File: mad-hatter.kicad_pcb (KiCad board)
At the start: 2 copper layers, 337.2 x 122.6 mm, 153 parts, among them U1 ATMEGA32U4, X1 XTAL_GND

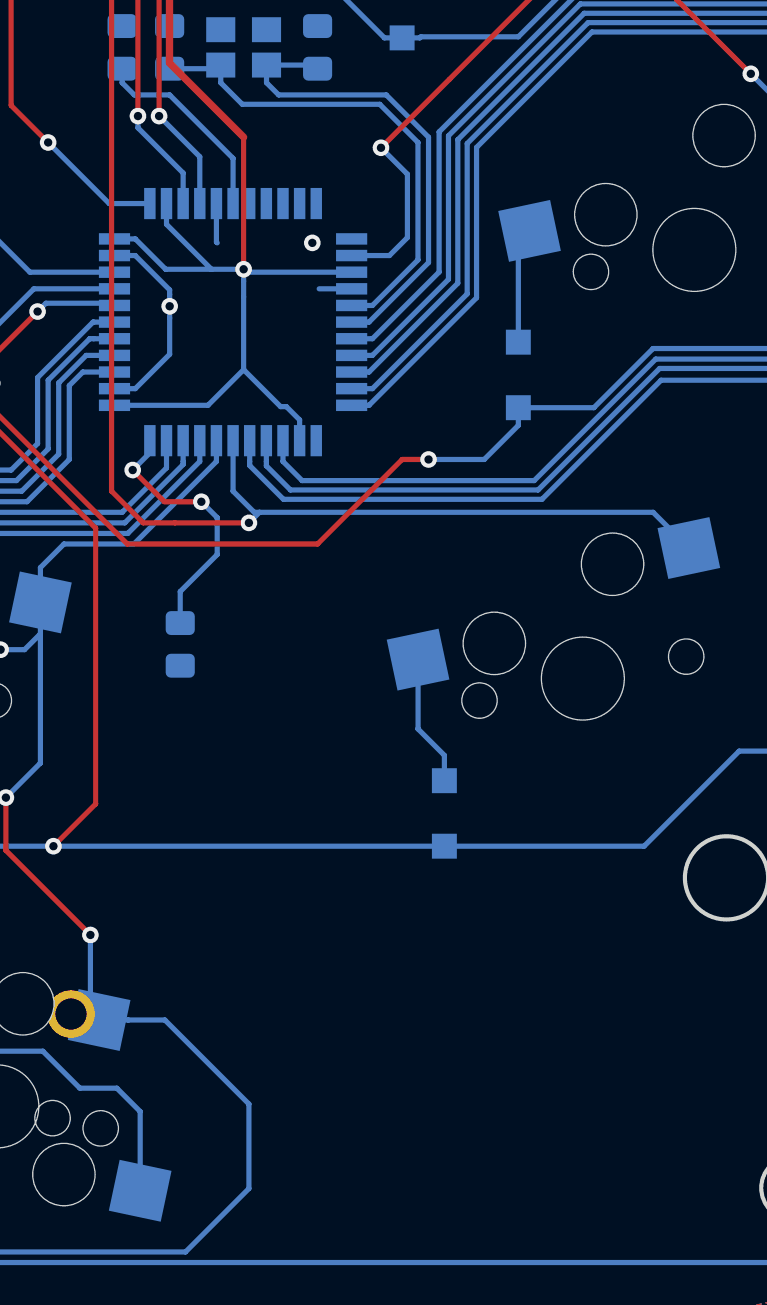
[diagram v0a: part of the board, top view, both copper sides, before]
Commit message: Starts adding ISP pads
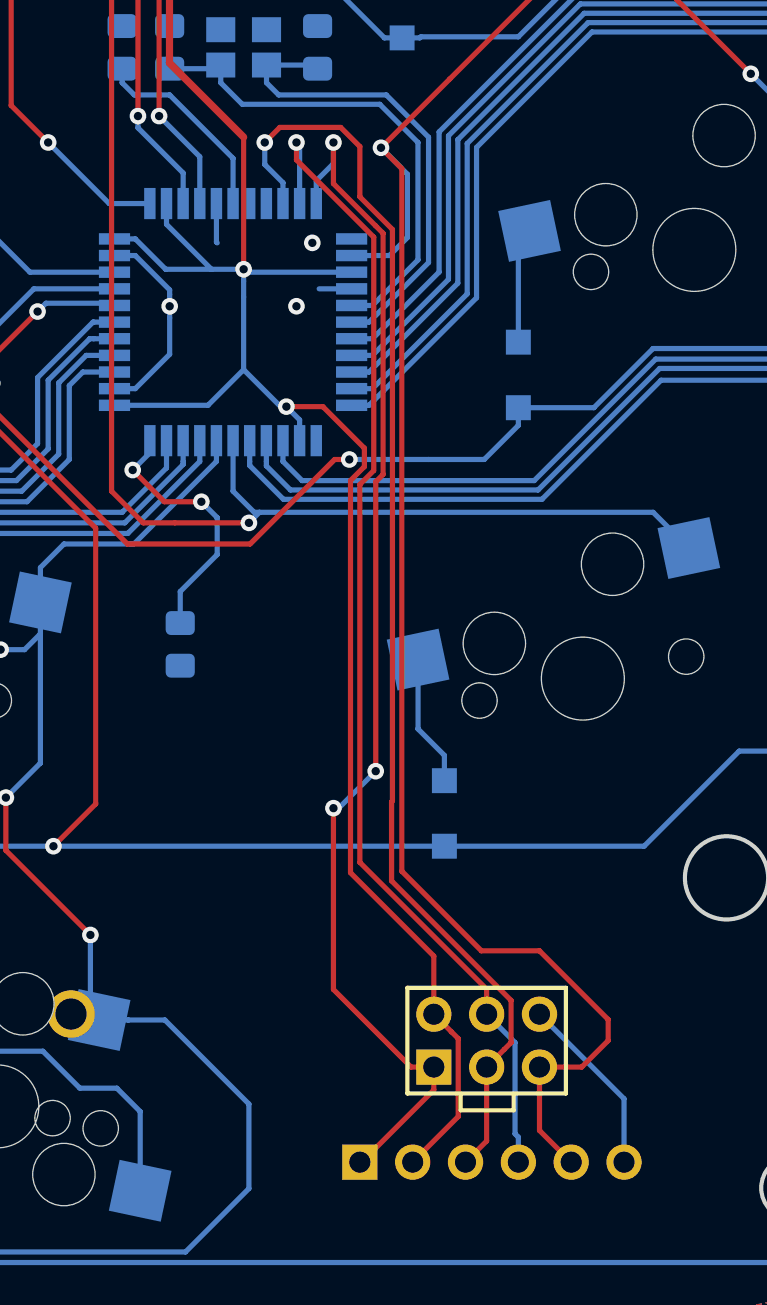
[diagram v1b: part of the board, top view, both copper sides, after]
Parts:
- added J1: AVR-ISP-6, keyboard_parts:AVR_ICSP_3x2, F.Cu at (308.9, 246.9)
- added P?: CONN_1, keyboard_parts:PIN_1, F.Cu at (315.5, 252.7)
- added P?: CONN_1, keyboard_parts:PIN_1, F.Cu at (312.9, 252.7)
- added P?: CONN_1, keyboard_parts:PIN_1, F.Cu at (310.4, 252.7)
- added P?: CONN_1, keyboard_parts:PIN_1, F.Cu at (307.8, 252.7)
- added P?: CONN_1, keyboard_parts:PIN_1_SQUARE, F.Cu at (302.8, 252.7)
- added P?: CONN_1, keyboard_parts:PIN_1, F.Cu at (305.3, 252.7)
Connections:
- net Net-(R1-Pad1) renamed RST
- U1 pad 10: Net-(U1-Pad10) -> MOSI
- U1 pad 11: Net-(U1-Pad11) -> MISO
- U1 pad 9: Net-(U1-Pad9) -> SCK
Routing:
- net SCK: track 0.00 -> 61.3 mm, vias 0 -> 1
- net MISO: track 0.00 -> 58.6 mm, vias 0 -> 3
- net RST: track 83.0 -> 141.1 mm
- net MOSI: track 0.00 -> 57.0 mm, vias 0 -> 1
- net VUSB: track 117.6 -> 159.8 mm, vias 3 -> 4
- net GND: track 34.3 -> 43.1 mm, vias 5 -> 6
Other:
- board text added: "GND"
- board text added: "MISO"
- board text added: "MOSI"
- board text added: "RST"
- board text added: "SCK"
- board text added: "VUSB"

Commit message: Fixes crystal connection; improves matrix; adds fuse
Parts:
- removed USB1: USB_mini_micro_B, keyboard_parts:USB_miniB_hirose_5S8
- added F1: 500mA, Fuse:Fuse_1206_3216Metric_Pad1.42x1.75mm_HandSolder, B.Cu at (301.5, 151.5)
- added J1: XM7D-0512, OMRON_XM7D-0512, F.Cu at (298.3, 147.2)
- U1: footprint SMD_ICs:TQFP44 -> keyboard_parts:QFP44_reflow
- X1: value XTAL_GND -> 16MHz
- moved C6 27.0 mm to (292.7, 194.5)
- moved C3 27.0 mm to (292.7, 200.6)
- moved C4 27.0 mm to (292.7, 198.5)
- moved C5 27.0 mm to (292.7, 196.5)
- moved C7 27.0 mm to (292.7, 192.4)
- moved C2 18.7 mm to (303.3, 215.1), turned to 0 degrees
- moved R4 17.6 mm to (280.3, 216.9), turned to 270 degrees
- moved X1 14.0 mm to (303.3, 211.7), turned to 270 degrees
- moved C1 9.49 mm to (303.3, 208.3), turned to 180 degrees
- moved D_CAPS_LOCK1 6.03 mm to (155.3, 200.2)
- moved C8 5.89 mm to (297.1, 200.5), turned to 180 degrees
- moved U1 5.84 mm to (290.8, 212.2)
- moved D_BSLSH2 5.33 mm to (453.0, 166.0)
- moved D_10 5.13 mm to (238.8, 239.1), turned to 78 degrees
- moved D_PGDN1 5.00 mm to (131.4, 198.4)
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- renumbered J1 to J2
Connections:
- C3 pad 1: VUSB -> +5V
- C4 pad 1: VUSB -> +5V
- C5 pad 1: VUSB -> +5V
- C6 pad 1: VUSB -> +5V
- C7 pad 1: VUSB -> +5V
- D_PGDN1 pad 1: ROW2 -> ROW3
- D_PGUP1 pad 1: ROW1 -> ROW2
- D_PRSCR1 pad 1: ROW0 -> ROW1
- J2 pad 2: VUSB -> +5V
- K_0 pad 1: COL11 -> COL10
- K_1 pad 1: COL2 -> COL1
- K_13 pad 1: COL15 -> COL14
- K_2 pad 1: COL3 -> COL2
- K_3 pad 1: COL4 -> COL3
- K_4 pad 1: COL5 -> COL4
- K_5 pad 1: COL6 -> COL5
- K_6 pad 1: COL7 -> COL6
- K_7 pad 1: COL8 -> COL7
- K_8 pad 1: COL9 -> COL8
- K_9 pad 1: COL10 -> COL9
- K_BACKSPACE1 pad 1: COL14 -> COL13
- K_BACKSPACE2 pad 2: COL14 -> COL13
- K_BSLSH1 pad 1: COL15 -> COL14
- K_BSLSH2 pad 1: COL15 -> COL14
- K_CTRL2 pad 1: COL15 -> COL14
- K_ENTER1 pad 1: COL14 -> COL13
- K_EQUAL1 pad 1: COL13 -> COL12
- K_H1 pad 1: COL8 -> COL7
- K_I1 pad 1: COL10 -> COL9
- K_J1 pad 1: COL9 -> COL8
- K_K1 pad 1: COL10 -> COL9
- K_L1 pad 1: COL11 -> COL10
- K_MINUS1 pad 1: COL12 -> COL11
- K_O1 pad 1: COL11 -> COL10
- K_P1 pad 1: COL12 -> COL11
- K_QUOTE1 pad 1: COL13 -> COL12
- K_SEMIC1 pad 1: COL12 -> COL11
- K_SHIFT2 pad 1: COL14 -> COL13
- K_SHIFT2_2 pad 2: COL14 -> COL13
- K_U1 pad 1: COL9 -> COL8
- K_Y1 pad 1: COL8 -> COL7
- K_[1 pad 1: COL13 -> COL12
- K_]1 pad 1: COL14 -> COL13
- K_`1 pad 1: COL1 -> COL0
- R1 pad 2: VUSB -> +5V
- U1 pad 14: VUSB -> +5V
- U1 pad 16: Net-(C2-Pad1) -> Net-(C1-Pad1)
- U1 pad 17: Net-(C1-Pad1) -> Net-(C2-Pad1)
- U1 pad 18: COL15 -> Net-(U1-Pad18)
- U1 pad 2: VUSB -> +5V
- U1 pad 24: VUSB -> +5V
- U1 pad 34: VUSB -> +5V
- U1 pad 36: COL2 -> ROW4
- U1 pad 37: COL1 -> ROW3
- U1 pad 38: COL0 -> COL2
- U1 pad 39: ROW4 -> COL1
- U1 pad 40: ROW3 -> COL0
- U1 pad 42: ROW1 -> Net-(U1-Pad42)
- U1 pad 44: VUSB -> +5V
- U1 pad 7: Net-(U1-Pad7) -> +5V
- U1 pad 8: Net-(U1-Pad8) -> ROW1
- X1 pad 2: Net-(C2-Pad1) -> GND
- X1 pad 3: GND -> Net-(C2-Pad1)
- X1 pad 4: (no net) -> GND
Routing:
- net COL15: track 271.1 -> 0.00 mm
- net GND: track 43.1 -> 266.6 mm, vias 6 -> 5
- net VUSB: track 159.8 -> 0.00 mm, vias 4 -> 0
- net +5V: track 0.00 -> 155.0 mm, vias 0 -> 6
- net COL13: track 182.3 -> 249.4 mm
- net ROW3: track 352.3 -> 417.0 mm
- net COL4: track 115.9 -> 142.1 mm, vias 6 -> 8
- net ROW0: track 365.4 -> 345.2 mm
- net COL3: track 143.3 -> 159.3 mm, vias 6 -> 8
- net Net-(C2-Pad1): track 23.8 -> 8.54 mm
- net COL0: track 211.8 -> 226.3 mm, vias 6 -> 3
- net Net-(C1-Pad1): track 23.2 -> 10.6 mm
- net COL7: track 88.7 -> 100.7 mm, vias 2 -> 6
- net COL14: track 259.4 -> 269.4 mm, vias 4 -> 2
- net ROW2: track 342.1 -> 351.1 mm, vias 2 -> 4
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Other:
- outline, holes or cut-outs redrawn
- net class Power added: clearance 0.2, trace_width 0.381, via_dia 0.8, via_drill 0.4

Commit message: Improvements
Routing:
- net GND: vias 5 -> 6
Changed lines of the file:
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@@
     (thickness 1.6)
     (drawings 626)
-    (tracks 1389)
+    (tracks 1390)
     (zones 0)
     (modules 161)
@@
   (segment (start 307.929464 232.664) (end 307.929464 241.508464) (width 0.381) (layer F.Cu) (net 1))
   (via (at 307.929464 232.664) (size 0.8) (drill 0.4) (layers F.Cu B.Cu) (net 1))
+  (via (at 289.433 212.598) (size 0.8) (drill 0.4) (layers F.Cu B.Cu) (net 1))
   (segment (start 181.655 160.813) (end 181.61 160.858) (width 0.25) (layer B.Cu) (net 2))
   (segment (start 181.655 155.55625) (end 181.655 160.813) (width 0.25) (layer B.Cu) (net 2))
@@
   (segment (start 299.339 200.533) (end 299.72 200.914) (width 0.25) (layer B.Cu) (net 19))
   (segment (start 299.72 200.914) (end 299.72 202.311) (width 0.25) (layer B.Cu) (net 19))
-  (segment (start 299.320001 202.710999) (end 294.367001 202.710999) (width 0.25) (layer F.Cu) (net 19))
-  (segment (start 299.72 202.311) (end 299.320001 202.710999) (width 0.25) (layer F.Cu) (net 19))
-  (via (at 290.83 203.962) (size 0.8) (drill 0.4) (layers F.Cu B.Cu) (net 19))
-  (segment (start 294.367001 202.710999) (end 293.116 203.962) (width 0.25) (layer F.Cu) (net 19))
-  (segment (start 293.116 203.962) (end 290.83 203.962) (width 0.25) (layer F.Cu) (net 19))
+  (via (at 290.83 204.724) (size 0.8) (drill 0.4) (layers F.Cu B.Cu) (net 19))
   (segment (start 290.83 204.527685) (end 290.83 206.517) (width 0.25) (layer B.Cu) (net 19))
-  (segment (start 290.83 203.962) (end 290.83 204.527685) (width 0.25) (layer B.Cu) (net 19))
+  (segment (start 294.367001 202.710999) (end 299.320001 202.710999) (width 0.25) (layer F.Cu) (net 19))
+  (segment (start 290.83 204.724) (end 292.354 204.724) (width 0.25) (layer F.Cu) (net 19))
+  (segment (start 299.320001 202.710999) (end 299.72 202.311) (width 0.25) (layer F.Cu) (net 19))
+  (segment (start 292.354 204.724) (end 294.367001 202.710999) (width 0.25) (layer F.Cu) (net 19))
   (segment (start 450.59375 214.20625) (end 450.59375 212.70625) (width 0.25) (layer B.Cu) (net 20))
   (segment (start 450.59375 214.506584) (end 450.59375 214.20625) (width 0.25) (layer B.Cu) (net 20))
@@
   (segment (start 287.63 204.191) (end 286.385 202.946) (width 0.381) (layer B.Cu) (net 100))
   (segment (start 286.385 202.946) (end 287.147 202.184) (width 0.381) (layer F.Cu) (net 100))
-  (via (at 291.649666 203.073) (size 0.8) (drill 0.4) (layers F.Cu B.Cu) (net 100))
-  (segment (start 290.760666 202.184) (end 291.649666 203.073) (width 0.381) (layer F.Cu) (net 100))
+  (via (at 291.649666 202.184) (size 0.8) (drill 0.4) (layers F.Cu B.Cu) (net 100))
   (segment (start 287.147 202.184) (end 290.760666 202.184) (width 0.381) (layer F.Cu) (net 100))
   (segment (start 291.649666 200.567571) (end 291.649666 203.073) (width 0.381) (layer B.Cu) (net 100))
@@
   (segment (start 300.19625 244.82425) (end 303.149 244.82425) (width 0.381) (layer B.Cu) (net 100))
   (segment (start 297.053 241.681) (end 300.19625 244.82425) (width 0.381) (layer B.Cu) (net 100))
+  (segment (start 291.083981 202.184) (end 290.760666 202.184) (width 0.381) (layer F.Cu) (net 100))
+  (segment (start 291.649666 202.184) (end 291.083981 202.184) (width 0.381) (layer F.Cu) (net 100))
   (segment (start 299.884997 151.385497) (end 300.0105 151.511) (width 0.381) (layer B.Cu) (net 101))
   (segment (start 299.884997 148.093) (end 299.884997 151.385497) (width 0.381) (layer B.Cu) (net 101))

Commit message: Various fixes:
- changes footprints to acheron
- routing fixes
- reorder ISP pins
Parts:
- D_0, D_1, D_2, D_3, D_4, D_5, D_6, D_7, D_8, D_9, D_A1, D_ALT1, D_ALT2, D_B1, D_B2, D_BACKSPACE1, D_BSLSH1, D_BSLSH2, D_C1, D_CAPS_LOCK1, D_COMMA1, D_CTRL1, D_CTRL2, D_D1, D_DOT1, D_E1, D_ENTER1, D_EQUAL1, D_F1, D_G1, D_H1, D_I1, D_J1, D_K1, D_L1, D_M1, D_MINUS1, D_N1, D_O1, D_P1, D_PGDN1, D_PGUP1, D_PRSCR1, D_Q1, D_QUOTE1, D_R1, D_S1, D_SEMIC1, D_SHIFT1, D_SHIFT2, D_SLASH1, D_T1, D_TAB1, D_U1, D_V1, D_W1, D_X1, D_Y1, D_Z1, D_[1, D_]1, D_`1: footprint keyboard_parts:D_SOD123_hand -> acheronComponents:D_SOD-123
- D_FN1: renamed from D_13; footprint keyboard_parts:D_SOD123_hand -> acheronComponents:D_SOD-123
- D_GUI1: renamed from D_11; footprint keyboard_parts:D_SOD123_hand -> acheronComponents:D_SOD-123
- D_SPC1: renamed from D_10; footprint keyboard_parts:D_SOD123_hand -> acheronComponents:D_SOD-123
- D_SPC2: renamed from D_12; footprint keyboard_parts:D_SOD123_hand -> acheronComponents:D_SOD-123
- F1: value 500mA -> 1A
- J1: value XM7D-0512 -> USB_B_Mini; footprint OMRON_XM7D-0512 -> acheronConnectors:miniB_connector
- J2: moved to B.Cu
- K_0, K_1, K_2, K_3, K_4, K_5, K_6, K_7, K_8, K_9, K_A1, K_ALT1, K_ALT2, K_B1, K_B2, K_BACKSPACE1, K_BACKSPACE2, K_BSLSH1, K_BSLSH2, K_C1, K_CAPS_LOCK1, K_CAPS_LOCK1_2, K_COMMA1, K_CTRL1, K_CTRL2, K_D1, K_DOT1, K_E1, K_ENTER1, K_EQUAL1, K_F1, K_G1, K_H1, K_I1, K_J1, K_K1, K_L1, K_M1, K_MINUS1, K_N1, K_O1, K_P1, K_PGDN1, K_PGUP1, K_PRSCR1, K_Q1, K_QUOTE1, K_R1, K_S1, K_SEMIC1, K_SHIFT1, K_SHIFT2, K_SHIFT2_2, K_SLASH1, K_T1, K_TAB1, K_U1, K_V1, K_W1, K_X1, K_Y1, K_Z1, K_[1, K_]1, K_`1: footprint keyswitches:Kailh_socket -> acheronKeyboardSwitches:MX100H; moved to B.Cu
- K_FN1: renamed from K_13; footprint keyswitches:Kailh_socket -> acheronKeyboardSwitches:MX100H; moved to B.Cu
- K_GUI1: renamed from K_11; footprint keyswitches:Kailh_socket -> acheronKeyboardSwitches:MX100H; moved to B.Cu
- K_GUI1_2: renamed from K_11_2; footprint keyswitches:Kailh_socket_optional -> acheronKeyboardSwitches:MX100H; moved to B.Cu
- K_SPC1: renamed from K_10; footprint keyswitches:Kailh_socket -> acheronKeyboardSwitches:MX100H; moved to B.Cu
- K_SPC1_2: renamed from K_10_2; footprint keyswitches:Kailh_socket_optional -> acheronKeyboardSwitches:MX100H; moved to B.Cu
- K_SPC2: renamed from K_12; footprint keyswitches:Kailh_socket -> acheronKeyboardSwitches:MX100H; moved to B.Cu
- RSW1: footprint Button_Switch_SMD:SW_SPST_TL3342 -> acheronHardware:smdPushBtn
- moved J1 0.67 mm to (298.3, 146.5), turned to 180 degrees
- moved J2 0.16 mm to (305.6, 246.0)
- turned K_0 to 192 degrees
- turned K_1 to 180 degrees
- turned K_2 to 180 degrees
- turned K_3 to 168 degrees
- turned K_4 to 168 degrees
- turned K_5 to 168 degrees
- turned K_6 to 168 degrees
- turned K_7 to 192 degrees
- turned K_8 to 192 degrees
- turned K_9 to 192 degrees
- turned K_A1 to 180 degrees
- turned K_ALT1 to 168 degrees
- turned K_ALT2 to 192 degrees
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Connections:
- P? pad 6: GND -> RST
- P? pad 5: RST -> GND
- P? pad 4: MOSI -> SCK
- P? pad 3: SCK -> MOSI
- P? pad 1: MISO -> +5V
- P? pad 2: VUSB -> MISO
- U1 pad 29: COL6 -> ROW4
- U1 pad 30: COL5 -> ROW3
- U1 pad 31: COL4 -> COL6
- U1 pad 32: COL3 -> COL5
- U1 pad 36: ROW4 -> COL4
- U1 pad 37: ROW3 -> COL3
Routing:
- net GND: track 266.6 -> 107.0 mm, vias 6 -> 2
- net COL3: track 159.3 -> 128.9 mm, vias 8 -> 4
- net COL4: track 142.1 -> 112.1 mm, vias 8 -> 4
- net ROW2: track 351.1 -> 379.1 mm
- net ROW3: track 417.0 -> 392.0 mm
- net SCK: track 65.5 -> 86.4 mm
- net COL6: track 145.1 -> 127.3 mm, vias 8 -> 6
- net COL5: track 169.5 -> 153.3 mm, vias 8 -> 5
- net COL1: track 217.9 -> 232.7 mm, vias 8 -> 5
- net +5V: track 154.6 -> 164.2 mm, vias 6 -> 5
- net MOSI: track 64.1 -> 56.9 mm
- net COL9: track 178.1 -> 171.0 mm, vias 7 -> 5
- net ROW4: track 357.9 -> 352.1 mm, vias 2 -> 0
- net ROW0: track 345.2 -> 340.7 mm
- net COL8: track 137.6 -> 141.4 mm, vias 8 -> 5
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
